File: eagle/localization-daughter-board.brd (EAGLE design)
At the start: 65 x 30 mm, 23 parts, among them U1 LM340MP-5.0/NOPB, U2 RPI-ZERO, U3 LMS8117AMP-ADJ/NOPB, U4 TXS0101DCKR, U5 SN65HVD256DR, U6 STM32F042FXP

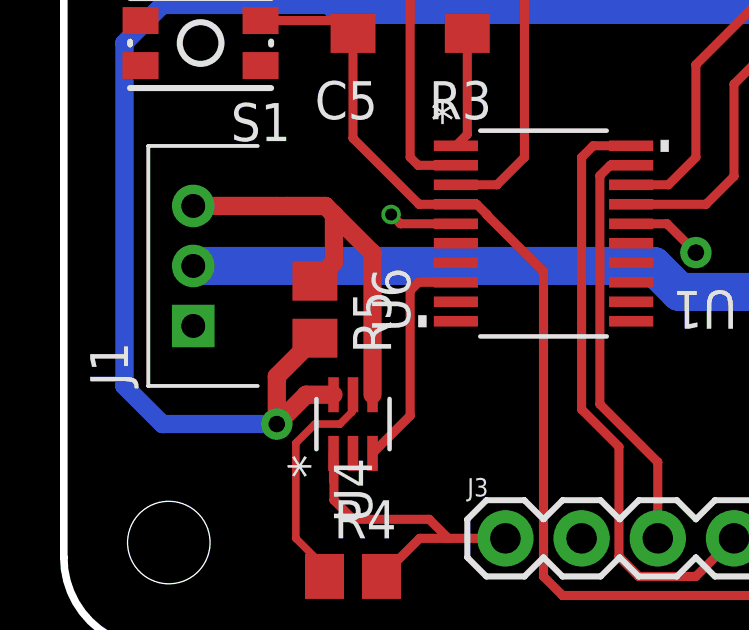
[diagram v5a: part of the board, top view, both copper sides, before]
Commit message: Removed redundant pull-up resistor
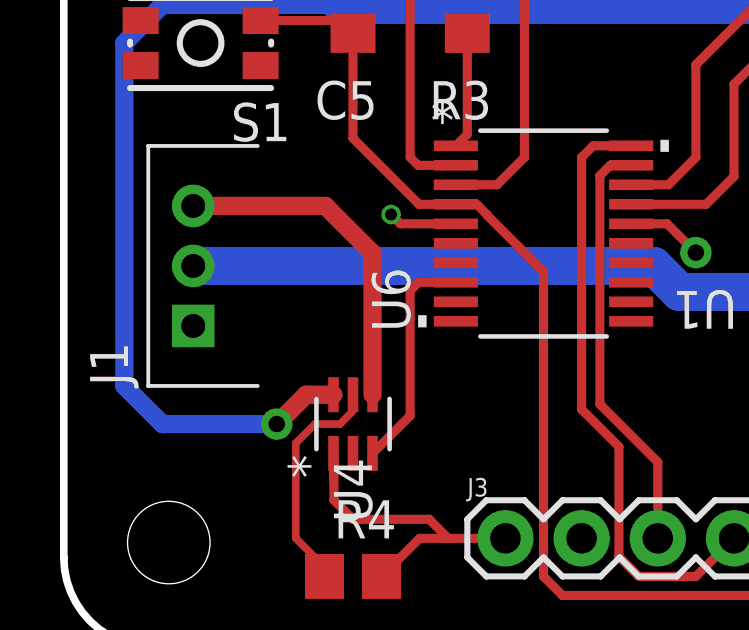
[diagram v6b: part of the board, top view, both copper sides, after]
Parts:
- removed R5: 10k, resistor:R0805
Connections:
- net +5V: no longer R5.2
- net UART_DYN_5V: no longer R5.1
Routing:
- net +5V: track 123.1 -> 119.7 mm
- net UART_DYN_5V: track 13.8 -> 11.3 mm
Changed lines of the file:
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@@
 <attribute name="NAME" x="34.29" y="12.7" size="1.27" layer="25" rot="R270"/>
-</element>
-<element name="R5" library="resistor" library_urn="urn:adsk.eagle:library:348" package="R0805" package3d_urn="urn:adsk.eagle:package:26059/1" value="10k" x="8.89" y="11.43" smashed="yes" rot="R270">
-<attribute name="NAME" x="10.16" y="12.065" size="1.27" layer="25" rot="R270"/>
 </element>
 <element name="R4" library="resistor" library_urn="urn:adsk.eagle:library:348" package="R0805" package3d_urn="urn:adsk.eagle:package:26059/1" value="10k" x="10.16" y="2.54"/>
@@
 <contactref element="C7" pad="1"/>
 <contactref element="C4" pad="1"/>
-<contactref element="R5" pad="2"/>
 <wire x1="31.2154" y1="12.38" x2="33.02" y2="12.38" width="1.27" layer="1"/>
 <wire x1="31.2154" y1="12.38" x2="29.605" y2="10.7696" width="1.27" layer="1"/>
@@
 <wire x1="2.54" y1="8.89" x2="3.81" y2="7.62" width="0.6096" layer="16"/>
 <wire x1="3.81" y1="7.62" x2="7.62" y2="7.62" width="0.6096" layer="16"/>
-<wire x1="8.89" y1="10.48" x2="7.62" y2="9.21" width="0.6096" layer="1"/>
-<wire x1="7.62" y1="9.21" x2="7.62" y2="7.62" width="0.6096" layer="1"/>
 </signal>
 <signal name="+3V3">
@@
 <contactref element="J1" pad="3"/>
 <contactref element="U4" pad="4"/>
-<contactref element="R5" pad="1"/>
-<wire x1="4.835" y1="14.89" x2="7.62" y2="14.89" width="0.6096" layer="1"/>
-<wire x1="7.62" y1="14.89" x2="7.97" y2="14.89" width="0.6096" layer="1"/>
-<wire x1="7.97" y1="14.89" x2="9.24" y2="14.89" width="0.6096" layer="1"/>
-<wire x1="9.525" y1="14.605" x2="9.24" y2="14.89" width="0.6096" layer="1"/>
-<wire x1="9.525" y1="14.605" x2="10.81" y2="13.32" width="0.6096" layer="1"/>
+<wire x1="4.835" y1="14.89" x2="9.24" y2="14.89" width="0.6096" layer="1"/>
+<wire x1="9.24" y1="14.89" x2="10.81" y2="13.32" width="0.6096" layer="1"/>
 <wire x1="10.81" y1="13.32" x2="10.81" y2="8.5979" width="0.6096" layer="1"/>
-<wire x1="8.89" y1="12.38" x2="9.525" y2="13.015" width="0.6096" layer="1"/>
-<wire x1="9.525" y1="13.015" x2="9.525" y2="14.605" width="0.6096" layer="1"/>
 </signal>
 <signal name="DYN_OE">
